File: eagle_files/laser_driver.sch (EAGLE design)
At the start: 40 parts, among them IC1 OKR-T/50-W12-C, IC2 7805, IC3 TLC272, J1 74650073R, J2 74650073R, J3 74650073R

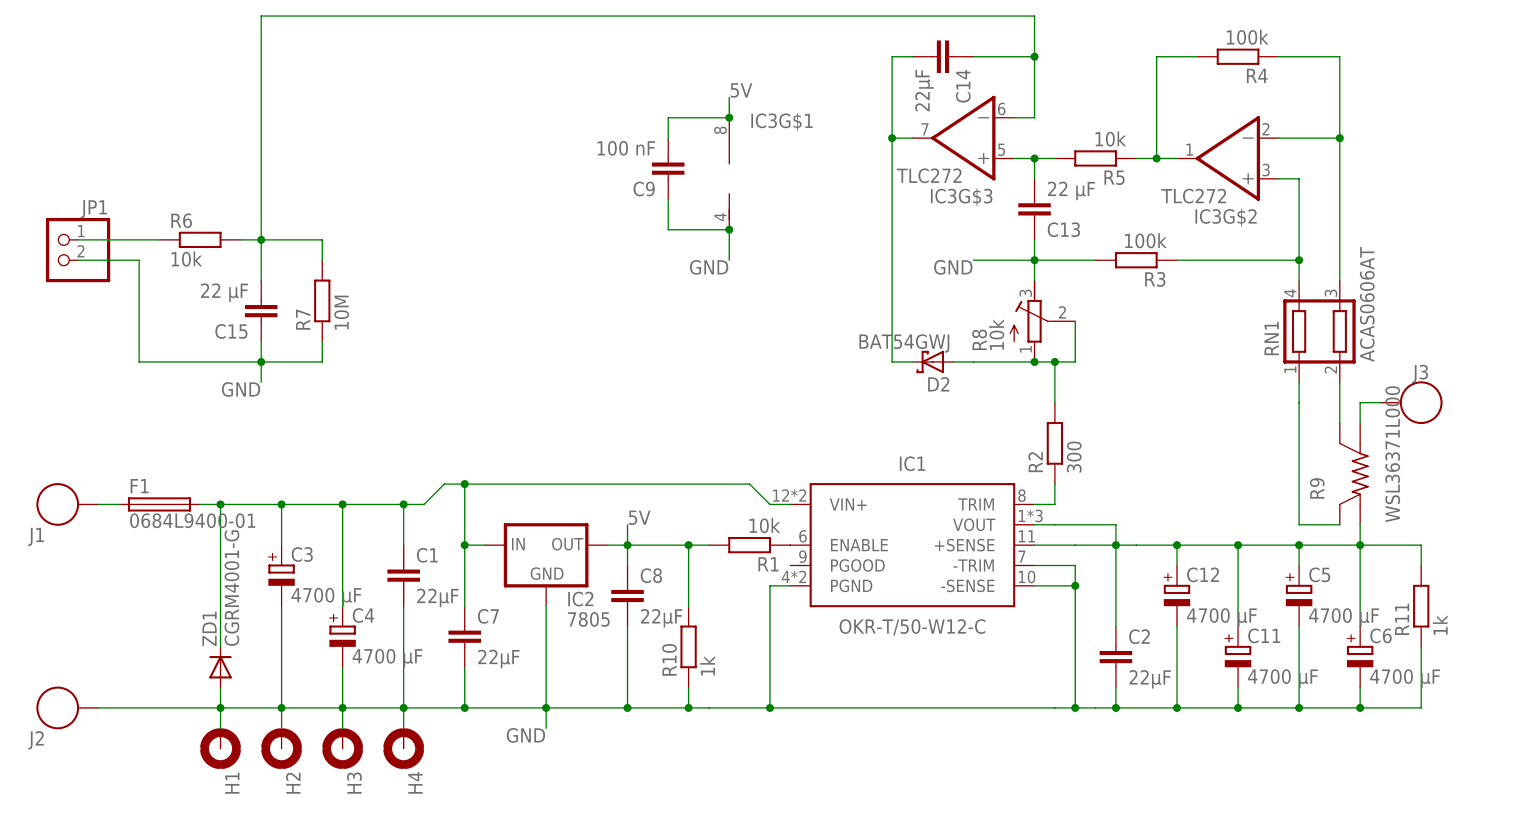
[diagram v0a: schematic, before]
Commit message: Improved stability, removed useless caps
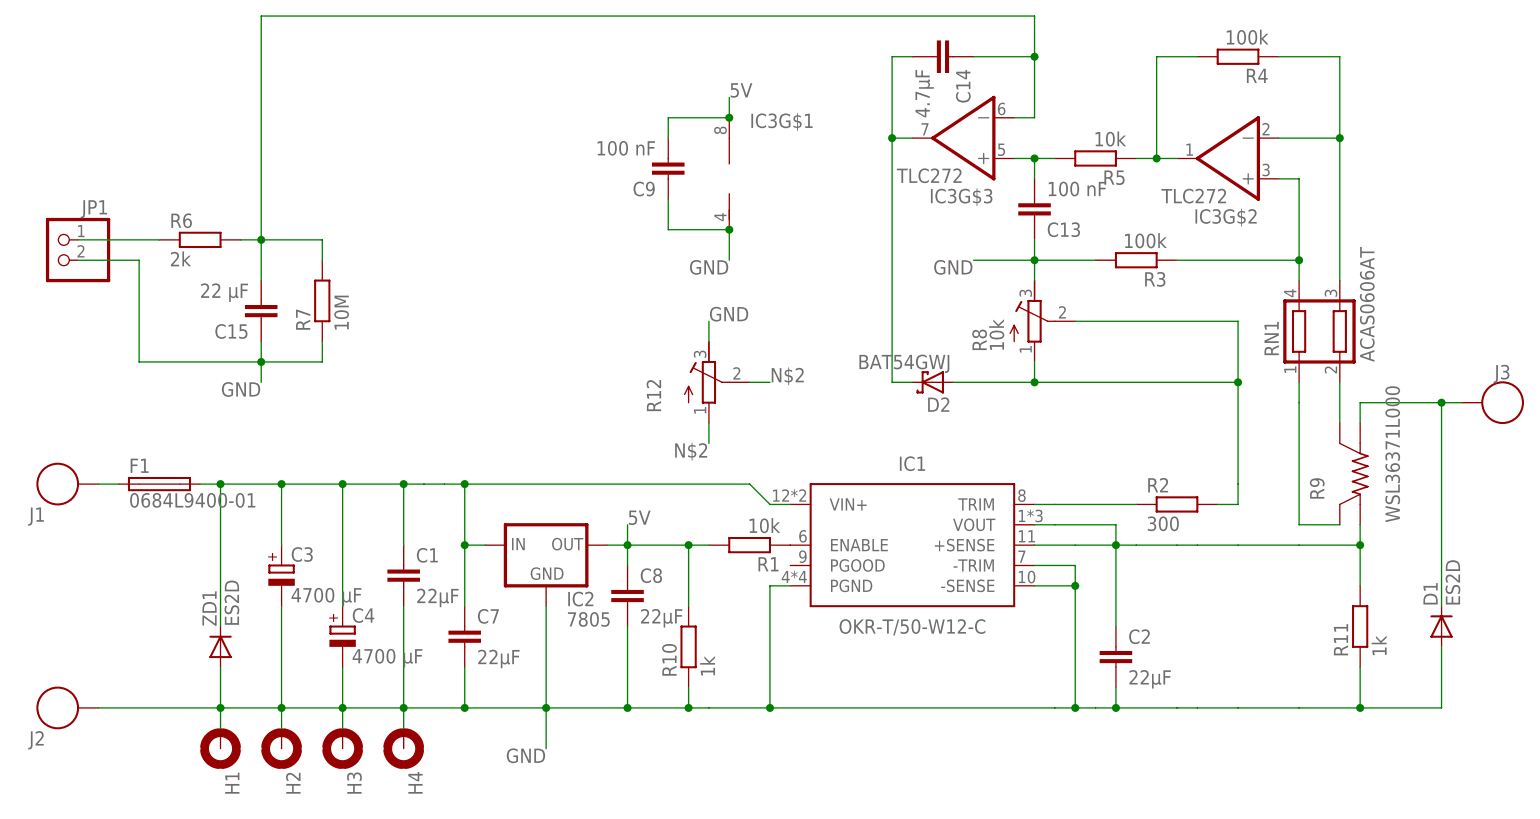
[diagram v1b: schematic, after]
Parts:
- removed C11, C12, C5, C6: 4700 µF, resistor:CPOL-EUE7.5-16
- added D1: ES2D, diode:ES2D
- added R12: (no value), rcl:R-TRIMM4G/J
- C1, C2, C7, C8: device resistor:C-EUC1210K -> rcl:C-EUC0805
- C13: value 22 µF -> 100 nF
- C14: value 22µF -> 4.7µF
- R6: value 10k -> 2k
- ZD1: value CGRM4001-G -> ES2D; device diode:CGRM4001-G -> diode:ES2D
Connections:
- net GND: now also D1.A, R12.E; no longer C11.-, C12.-, C5.-, C6.-
- net N$1: now also D1.C
- net N$2: now also R12.A, R12.S
- net N$4: no longer C11.+, C12.+, C5.+, C6.+
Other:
- moved on the sheet: D2, F1, J1, J3, R11, R2, ZD1

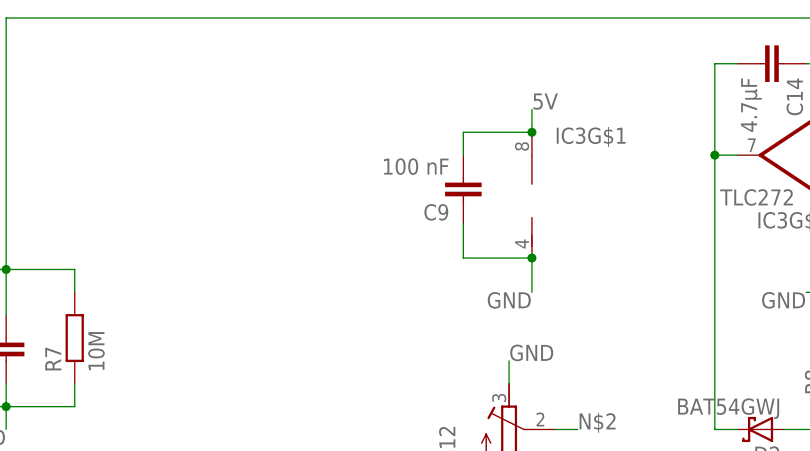
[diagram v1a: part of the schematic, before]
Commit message: Improved silk screen
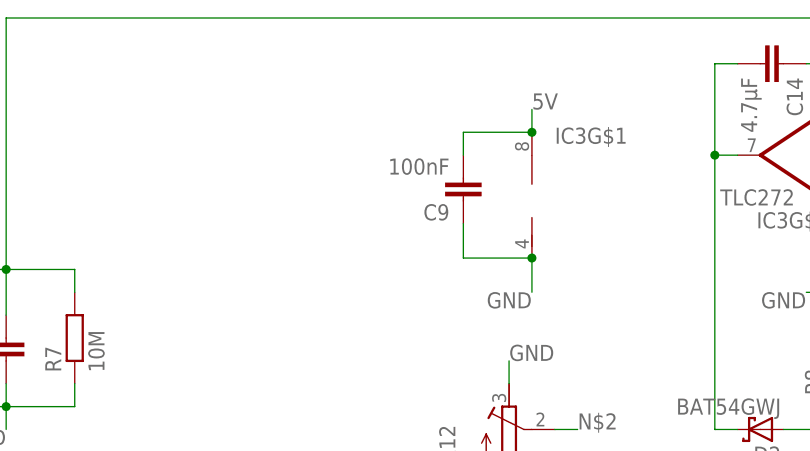
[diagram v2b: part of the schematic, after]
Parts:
- C9: value 100 nF -> 100nF
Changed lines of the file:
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@@
 <part name="R10" library="rcl" library_urn="urn:adsk.eagle:library:334" deviceset="R-EU_" device="R0805" package3d_urn="urn:adsk.eagle:package:23553/2" value="1k"/>
 <part name="R11" library="rcl" library_urn="urn:adsk.eagle:library:334" deviceset="R-EU_" device="R0805" package3d_urn="urn:adsk.eagle:package:23553/2" value="1k"/>
-<part name="C9" library="rcl" library_urn="urn:adsk.eagle:library:334" deviceset="C-EU" device="C0805" package3d_urn="urn:adsk.eagle:package:23617/2" value="100 nF"/>
+<part name="C9" library="rcl" library_urn="urn:adsk.eagle:library:334" deviceset="C-EU" device="C0805" package3d_urn="urn:adsk.eagle:package:23617/2" value="100nF"/>
 <part name="IC1" library="OKR-T-50-W12-C" deviceset="OKR-T/50-W12-C" device=""/>
 <part name="D1" library="diode" library_urn="urn:adsk.eagle:library:210" deviceset="ES2D" device="" package3d_urn="urn:adsk.eagle:package:43404/2"/>

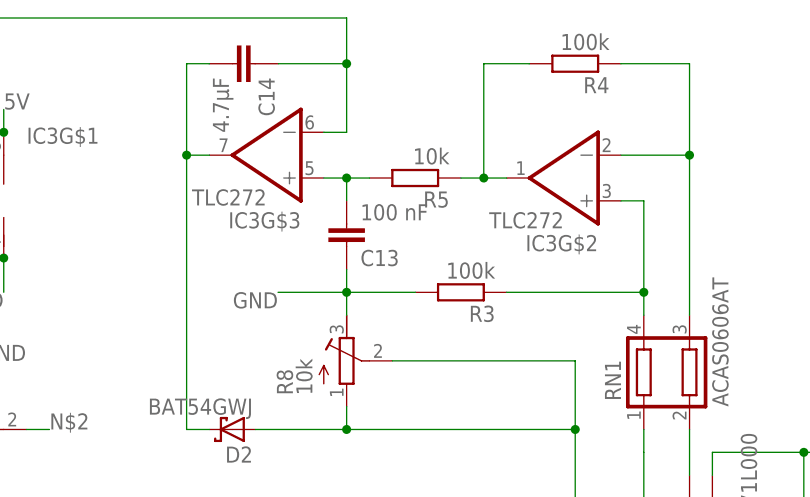
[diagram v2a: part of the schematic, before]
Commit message: Minor changes in component placement after assembly
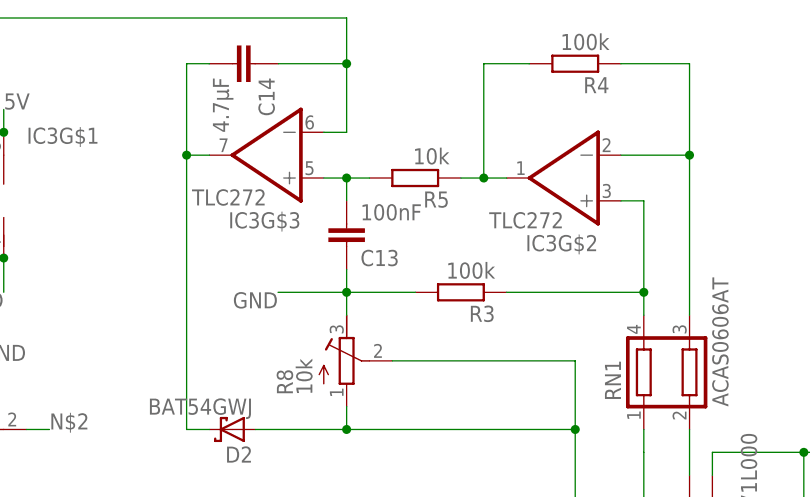
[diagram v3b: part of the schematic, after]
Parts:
- C13: value 100 nF -> 100nF
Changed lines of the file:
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@@
 <part name="R4" library="rcl" library_urn="urn:adsk.eagle:library:334" deviceset="R-EU_" device="R0805" package3d_urn="urn:adsk.eagle:package:23553/2" value="100k"/>
 <part name="R5" library="rcl" library_urn="urn:adsk.eagle:library:334" deviceset="R-EU_" device="R0805" package3d_urn="urn:adsk.eagle:package:23553/2" value="10k"/>
-<part name="C13" library="rcl" library_urn="urn:adsk.eagle:library:334" deviceset="C-EU" device="C0805" package3d_urn="urn:adsk.eagle:package:23617/2" value="100 nF"/>
+<part name="C13" library="rcl" library_urn="urn:adsk.eagle:library:334" deviceset="C-EU" device="C0805" package3d_urn="urn:adsk.eagle:package:23617/2" value="100nF"/>
 <part name="C14" library="rcl" library_urn="urn:adsk.eagle:library:334" deviceset="C-EU" device="C0805" package3d_urn="urn:adsk.eagle:package:23617/2" value="4.7µF"/>
 <part name="R6" library="rcl" library_urn="urn:adsk.eagle:library:334" deviceset="R-EU_" device="R0805" package3d_urn="urn:adsk.eagle:package:23553/2" value="2k"/>
